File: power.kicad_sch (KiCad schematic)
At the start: 58 parts, among them J4 Conn_01x02, J5 Conn_01x02, J6 Conn_01x02, Q29 AO3401, Q30 Q_NPN_BEC, T1 COMMON_MODE_CHOKE, U14 NCP1117ST33, U19 TPS54428DDA, U2 TPS54202

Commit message: Added some comments
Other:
- note added: "Some PI filters to reduce power line current ripples."
- note added: "There is no way to reset LED1642's internal counter other than using its Power-ON-Reset. This circuit pulls LED1642's VDD to the ground."
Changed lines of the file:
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@@
-(kicad_sch (version 20200820) (host eeschema "5.99.0-unknown-b0af66afc~103~ubuntu18.04.1")
+(kicad_sch (version 20200827) (generator eeschema)
   (page 9 10)
   (paper "A4")
@@
     (effects (font (size 1.27 1.27)) (justify left bottom))
   )
+  (text "Some PI filters to reduce power line current ripples."
+    (at 156.21 19.05 0)
+    (effects (font (size 1.27 1.27)) (justify right bottom))
+  )
   (text "12V" (at 166.37 22.86 0)
     (effects (font (size 1.27 1.27)) (justify left bottom))
   )
+  (text "There is no way to reset LED1642's internal counter other than using its Power-ON-Reset.\nThis circuit pulls LED1642's VDD to the ground."
+    (at 279.4 72.39 0)
+    (effects (font (size 1.27 1.27)) (justify right bottom))
+  )
   (label "DC_IN_N" (at 52.07 34.29 0)

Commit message: Fixed some comments; Added FB on SCL/SDA line
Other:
- note added: "NCP1117ST33 explicitly allows using ceramic capacitors at input and the output. I'm not sure that other compatible 1117 series regurators work well as this chip."
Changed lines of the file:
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@@
     (effects (font (size 1.27 1.27)) (justify left bottom))
+  )
+  (text "NCP1117ST33 explicitly allows using ceramic\ncapacitors at input and the output.\nI'm not sure that other compatible 1117 series \nregurators work well as this chip."
+    (at 140.97 69.85 0)
+    (effects (font (size 1.27 1.27)) (justify right bottom))
   )
   (text "LEDVDD  must be from min 3.1V to max 5.0V" (at 148.59 143.51 0)

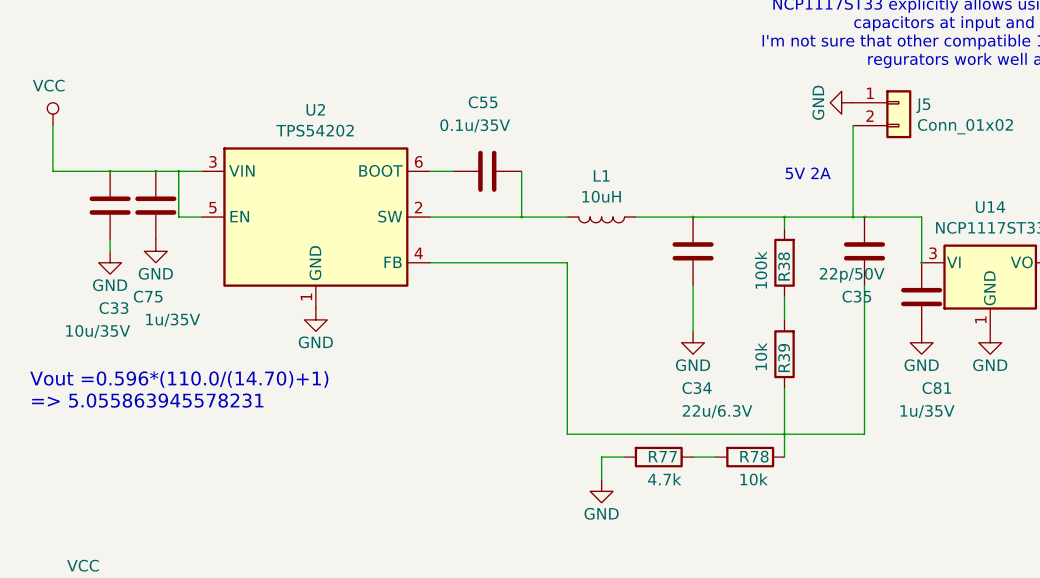
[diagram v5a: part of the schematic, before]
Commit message: Changed 5.05V buck regulator output to 4.65V (to decrease 3.3V LDO heat)
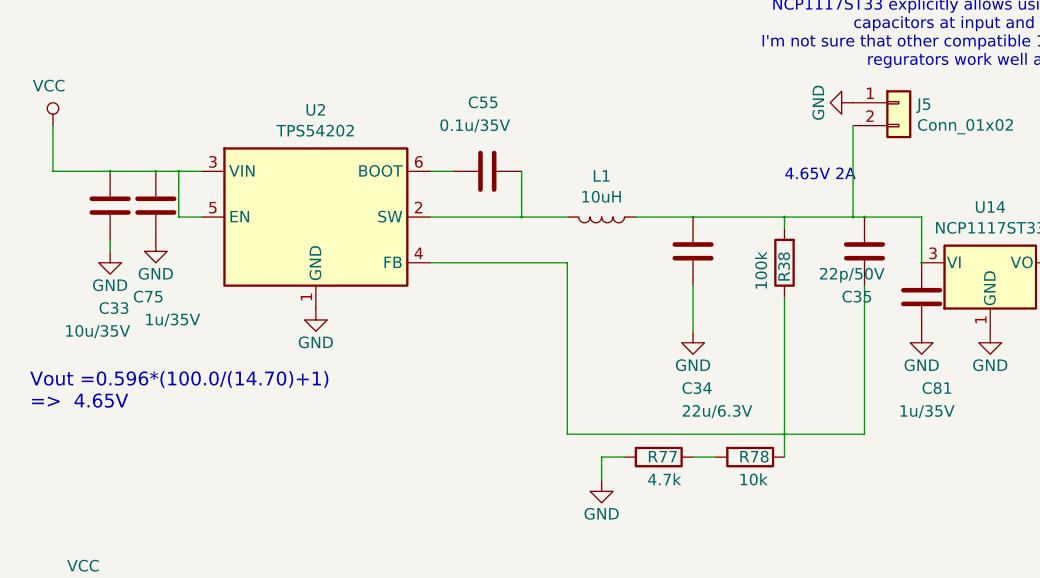
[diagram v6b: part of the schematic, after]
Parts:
- removed R39: 10k, Resistor_SMD:R_0603_1608Metric_Pad1.05x0.95mm_HandSolder, symbol dotmatrix_64x48-rescue:R-device
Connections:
- net at R38.1: now also C35.2, R78.1, U2.4 (FB)
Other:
- note added: "4.65V 2A"
- note added: "Vout =0.596*(100.0/(14.70)+1) => 4.65V"
- note removed: "5V 2A"
- note removed: "Vout =0.596*(110.0/(14.70)+1) => 5.055863945578231"
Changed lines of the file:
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@@
+    (stroke (width 0) (type solid) (color 0 0 0 0))
+  )
+  (wire (pts (xy 102.87 97.79) (xy 102.87 105.41))
     (stroke (width 0) (type solid) (color 0 0 0 0))
   )
@@
     (stroke (width 0) (type solid) (color 0 0 0 0))
   )
-  (text "Vout =0.596*(110.0/(14.70)+1)\n=> 5.055863945578231"
-    (at 19.05 107.95 0)
+  (text "Vout =0.596*(100.0/(14.70)+1)\n=>  4.65V" (at 19.05 107.95 0)
     (effects (font (size 1.524 1.524)) (justify left bottom))
   )
@@
     (effects (font (size 1.27 1.27)) (justify right bottom))
   )
-  (text "5V 2A" (at 102.87 82.55 0)
+  (text "4.65V 2A" (at 102.87 82.55 0)
     (effects (font (size 1.27 1.27)) (justify left bottom))
   )
@@
     (property "Datasheet" "" (id 3) (at 102.87 91.44 0))
   )
-  (symbol (lib_id "dotmatrix_64x48-rescue:R-device") (at 102.87 101.6 180) (unit 1)
-    (in_bom yes) (on_board yes)
-    (property "Reference" "R39" (id 0) (at 102.87 100.33 90)
-      (effects (font (size 1.27 1.27)) (justify left))
-    )
-    (property "Value" "10k" (id 1) (at 100.33 100.33 90)
-      (effects (font (size 1.27 1.27)) (justify left))
-    )
-    (property "Footprint" "Resistor_SMD:R_0603_1608Metric_Pad1.05x0.95mm_HandSolder" (id 2) (at 104.648 101.6 90)
-      (effects (font (size 1.27 1.27)) hide)
-    )
-    (property "Datasheet" "" (id 3) (at 102.87 101.6 0))
-  )
   (symbol (lib_id "dotmatrix_64x48-rescue:R-device") (at 237.49 102.87 90) (unit 1)

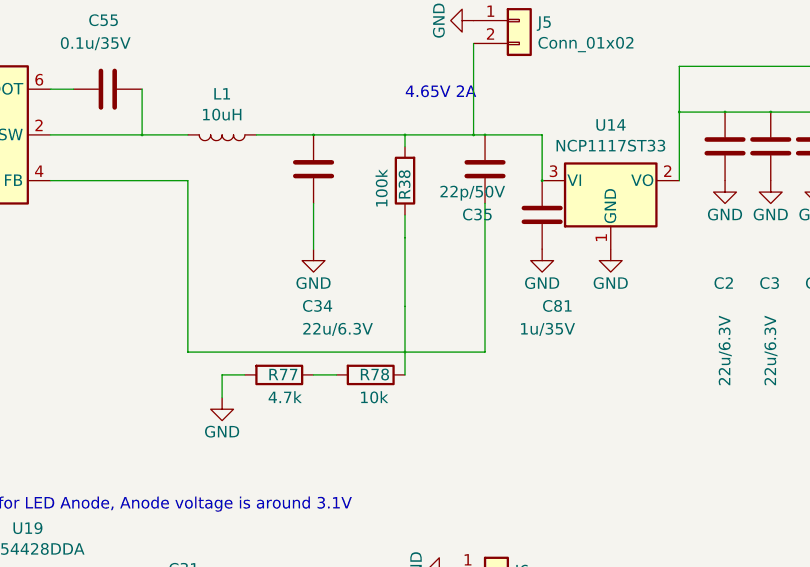
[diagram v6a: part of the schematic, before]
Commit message: Added J8.4; DRC clear
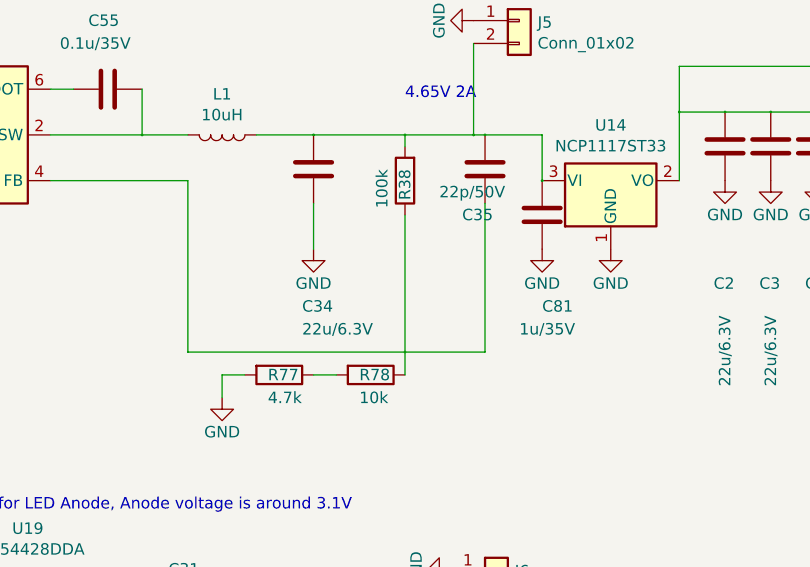
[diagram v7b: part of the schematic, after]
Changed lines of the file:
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@@
     (stroke (width 0) (type solid) (color 0 0 0 0))
   )
-  (wire (pts (xy 102.87 95.25) (xy 102.87 97.79))
-    (stroke (width 0) (type solid) (color 0 0 0 0))
-  )
-  (wire (pts (xy 102.87 97.79) (xy 102.87 105.41))
+  (wire (pts (xy 102.87 95.25) (xy 102.87 110.49))
     (stroke (width 0) (type solid) (color 0 0 0 0))
   )
@@
     (stroke (width 0) (type solid) (color 0 0 0 0))
   )
-  (wire (pts (xy 102.87 110.49) (xy 102.87 105.41))
-    (stroke (width 0) (type solid) (color 0 0 0 0))
-  )

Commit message: Moved leftside sensors to rightside; Unified old footprints to new footprints; DRC clear
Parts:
- L4: footprint Capacitors_SMD:C_0805_HandSoldering -> Capacitor_SMD:C_0805_2012Metric_Pad1.15x1.40mm_HandSolder
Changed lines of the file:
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@@
     (property "Reference" "L4" (id 0) (at 179.07 90.7288 90))
     (property "Value" "BLM21PG331SN 300R@100MHz" (id 1) (at 187.96 88.9 90))
-    (property "Footprint" "Capacitors_SMD:C_0805_HandSoldering" (id 2) (at 179.07 95.25 0)
+    (property "Footprint" "Capacitor_SMD:C_0805_2012Metric_Pad1.15x1.40mm_HandSolder" (id 2) (at 179.07 95.25 0)
       (effects (font (size 1.27 1.27)) hide)
     )
